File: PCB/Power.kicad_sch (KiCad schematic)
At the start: 29 parts, among them J12 PADROW-2, J2 USB-C, U4 USBLC6-2SC6, U8 AP2112K-3.3TRG1, U9 TPS54360

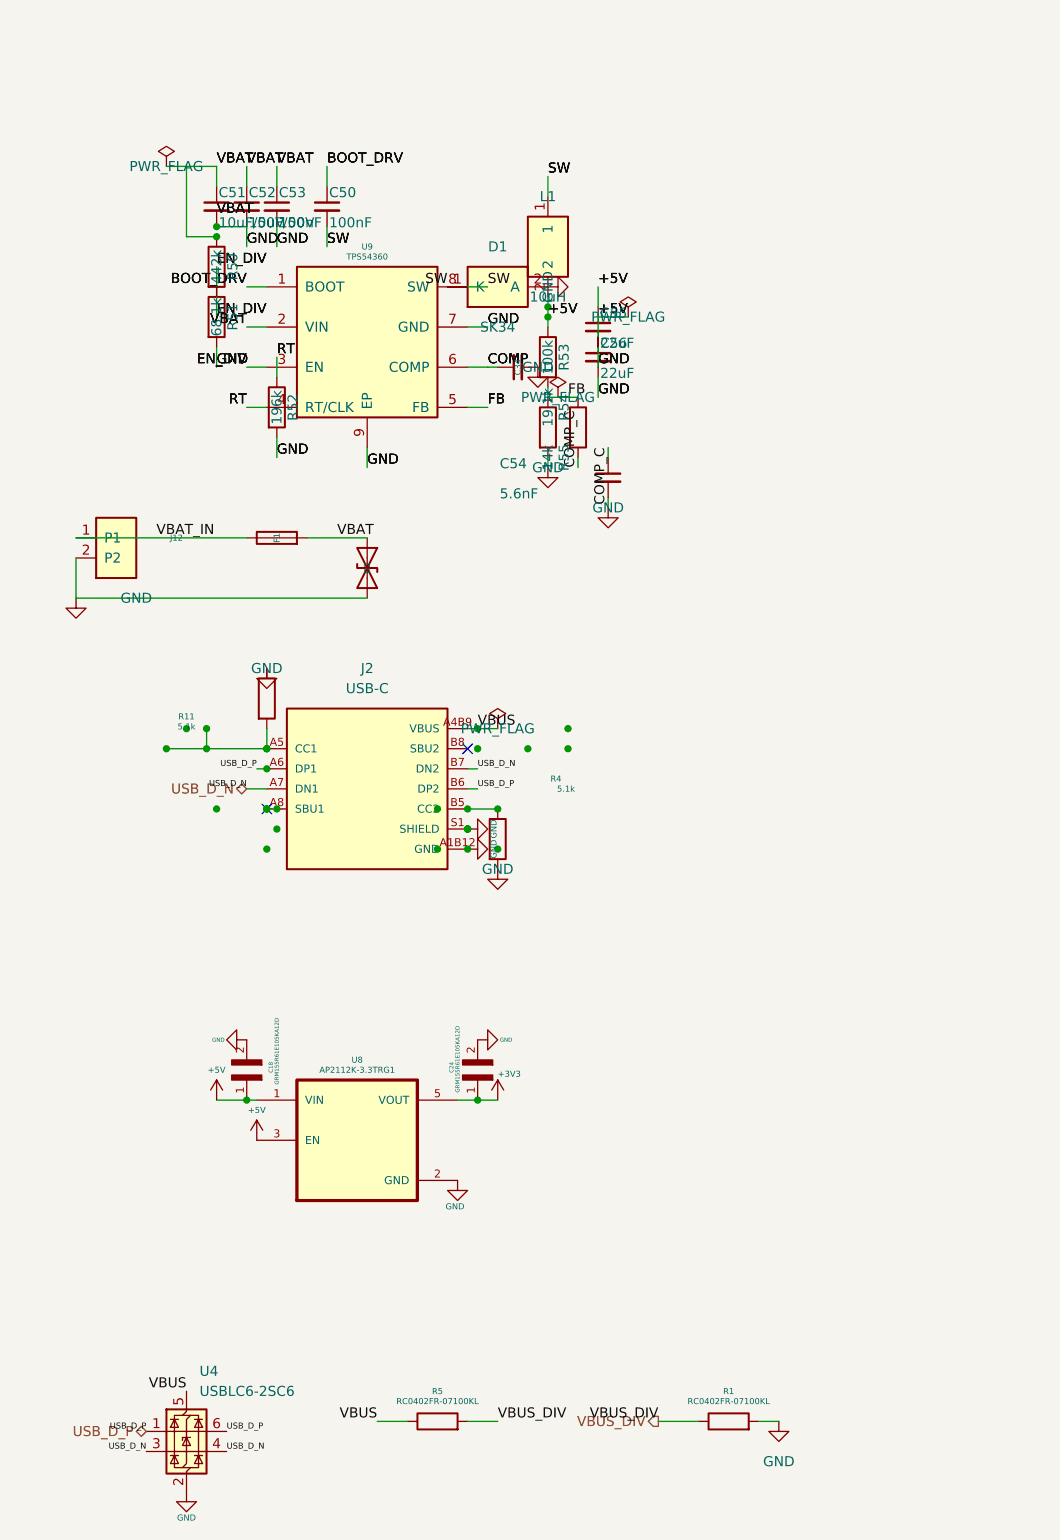
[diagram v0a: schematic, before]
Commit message: Repo polish: hardware-only OpenVCU (quad/plane/rover/boat), no firmware in git
- Rewrite README as multi-vehicle hardware repo with WIP status
- Git-ignore Firmware/ (out-of-tree until bring-up), *.docx
- Add MIT LICENSE and CONTRIBUTING.md
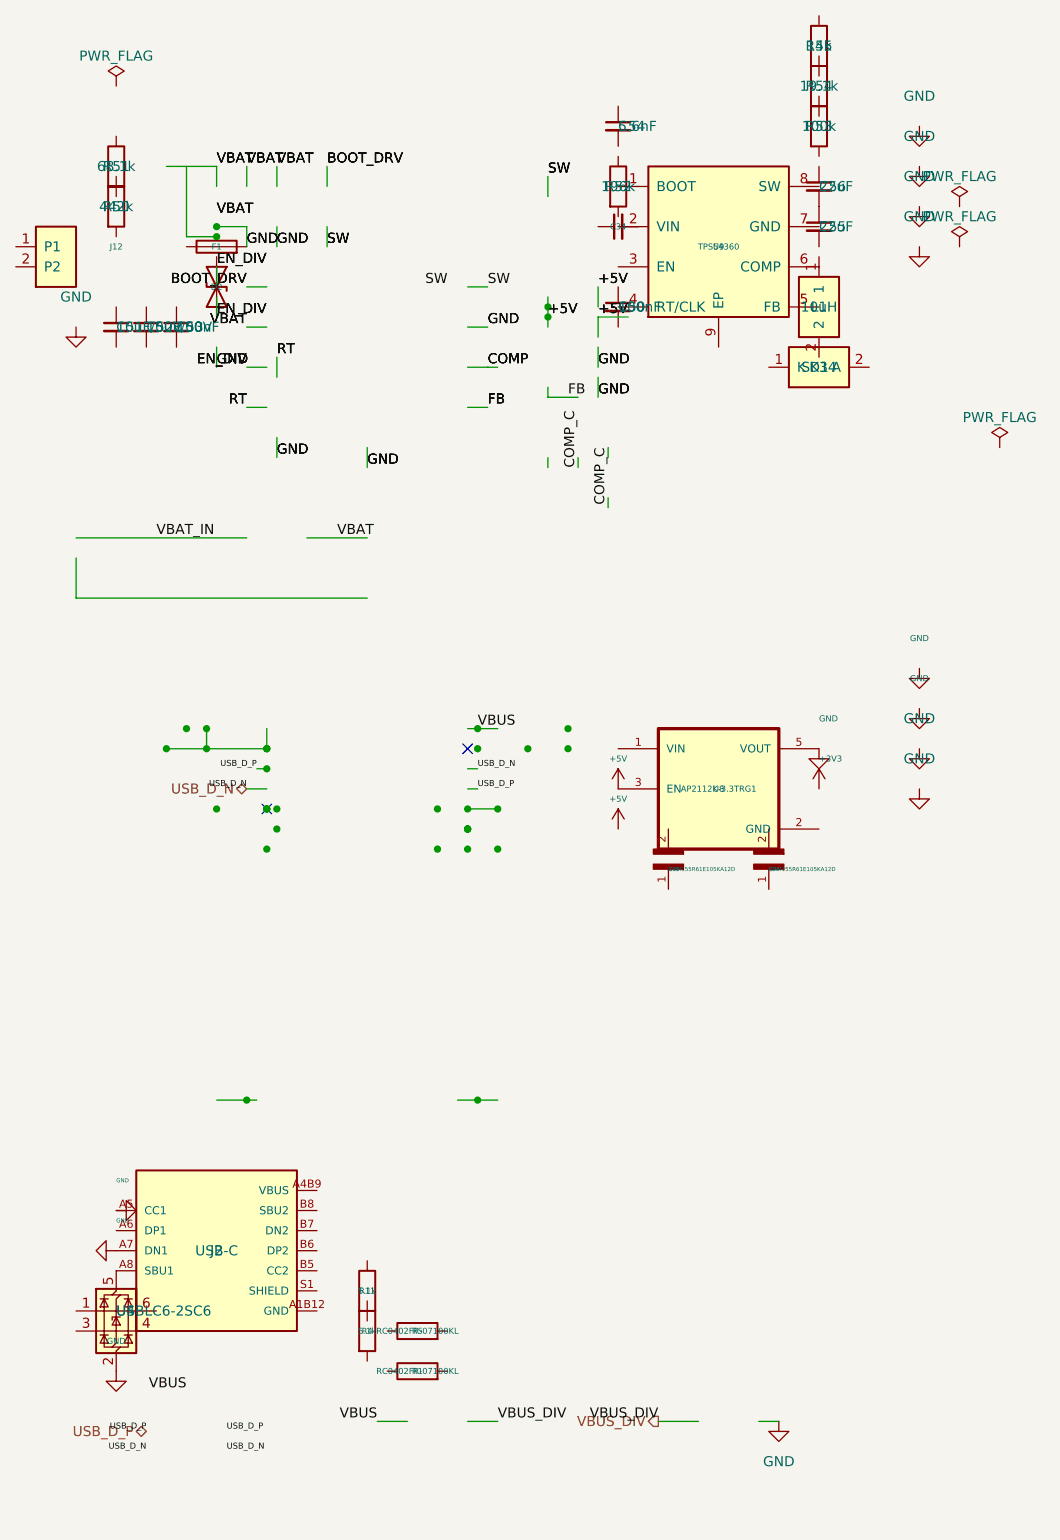
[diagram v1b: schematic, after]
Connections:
- net +3V3: no longer C24.1, U8.5 (VOUT)
- net +5V: no longer C18.1, C55.1, C56.1, L1.2, R53.1, U8.1 (VIN)
- net BOOT_DRV: no longer C50.1, U9.1 (BOOT)
- net COMP: no longer C34.1, U9.6 (COMP)
- net COMP_C: no longer C54.1, R55.2
- net EN_DIV: now also D2.2 (A2); no longer R50.2, R51.1, U9.3 (EN)
- net FB: no longer R53.2, R54.1, R55.1, U9.5 (FB)
- net GND: now also F1.2, J2.A5 (CC1), J2.A7 (DN1), U8.5 (VOUT); no longer C18.2, C24.2, C34.2, C51.2, C52.2, C53.2, C54.2, C55.2, C56.2, D1.2 (A), D2.2 (A2), J12.2 (P2), J2.S1 (SHIELD), J2.S2 (SHIELD), J2.S3 (SHIELD), J2.S4 (SHIELD), R1.2, R11.1, R4.2, R51.2, R52.2, R54.2, U8.2 (GND), U9.7 (GND), U9.9 (EP)
- net RT: no longer R52.1, U9.4 (RT/CLK)
- net SW: no longer C50.2, D1.1 (K), L1.1, U9.8 (SW)
- net USB_D_N: no longer J2.A7 (DN1), J2.B7 (DN2), U4.3 (I/O2), U4.4 (I/O2)
- net USB_D_P: no longer J2.A6 (DP1), J2.B6 (DP2), U4.1 (I/O1), U4.6 (I/O1)
- net VBAT: no longer C51.1, C52.1, C53.1, D2.1 (A1), F1.2, R50.1, U9.2 (VIN)
- net VBAT_IN: no longer F1.1, J12.1 (P1)
- net VBUS: no longer R5.1, U4.5 (VBUS)
- net VBUS_DIV: no longer R1.1, R5.2
- net at R11.2: no longer J2.A5 (CC1)
- net at J2.A8 (SBU1): now also U4.5 (VBUS)
- net at J2.B5 (CC2): no longer R4.1
- new net: J2.S1 (SHIELD), J2.S2 (SHIELD), J2.S3 (SHIELD), J2.S4 (SHIELD)
- new net: C55.1, C56.2
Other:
- moved on the sheet: C18, C24, C34, C50, C51, C52, C53, C54, C55, C56, D1, D2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
